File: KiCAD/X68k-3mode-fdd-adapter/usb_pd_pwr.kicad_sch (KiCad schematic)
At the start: 27 parts, among them J1001 Barrel_Jack_Switch, J1002 USB_C_Receptacle_USB2.0_16P, Q1001 FDS4935A, Q1002 FDS4935A, Q1003 FDS4935A, U1001 K7805M-1000R3, U1002 MCP1792x-5002xCB

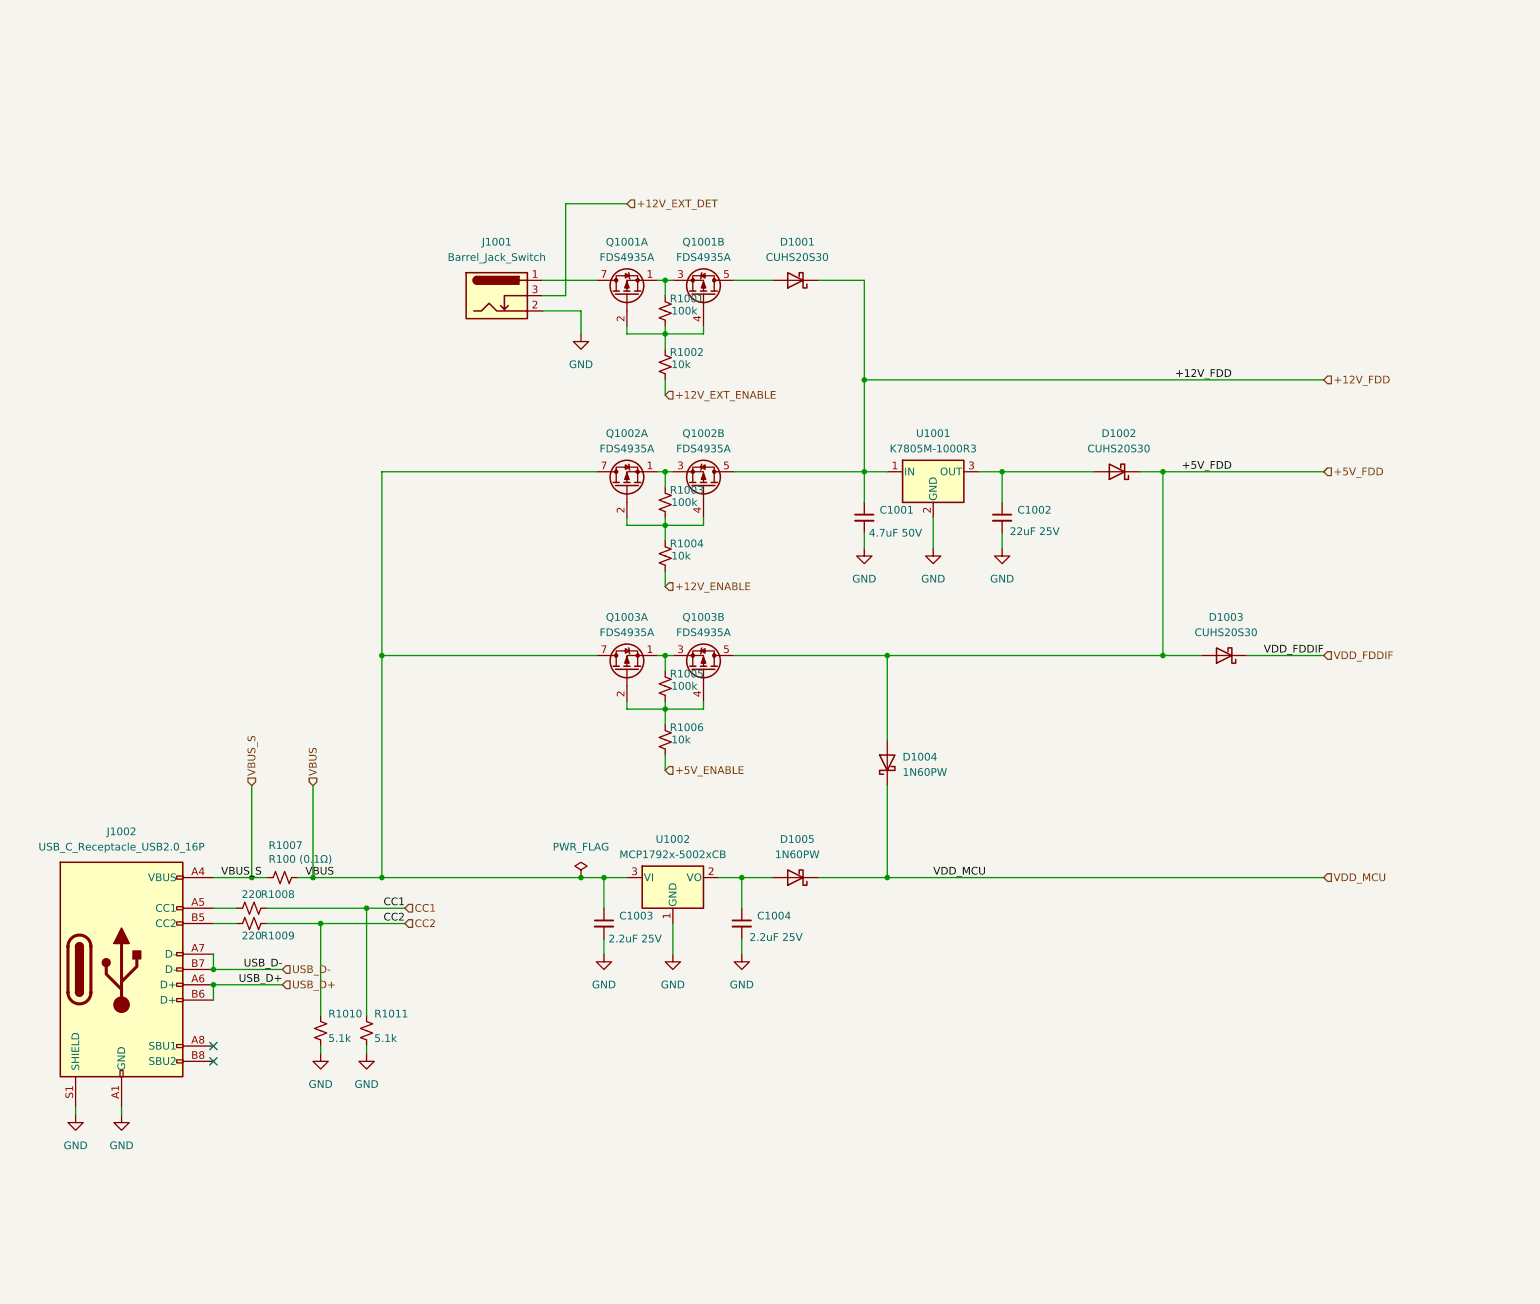
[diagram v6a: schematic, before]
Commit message: 電源周りの回路を修正
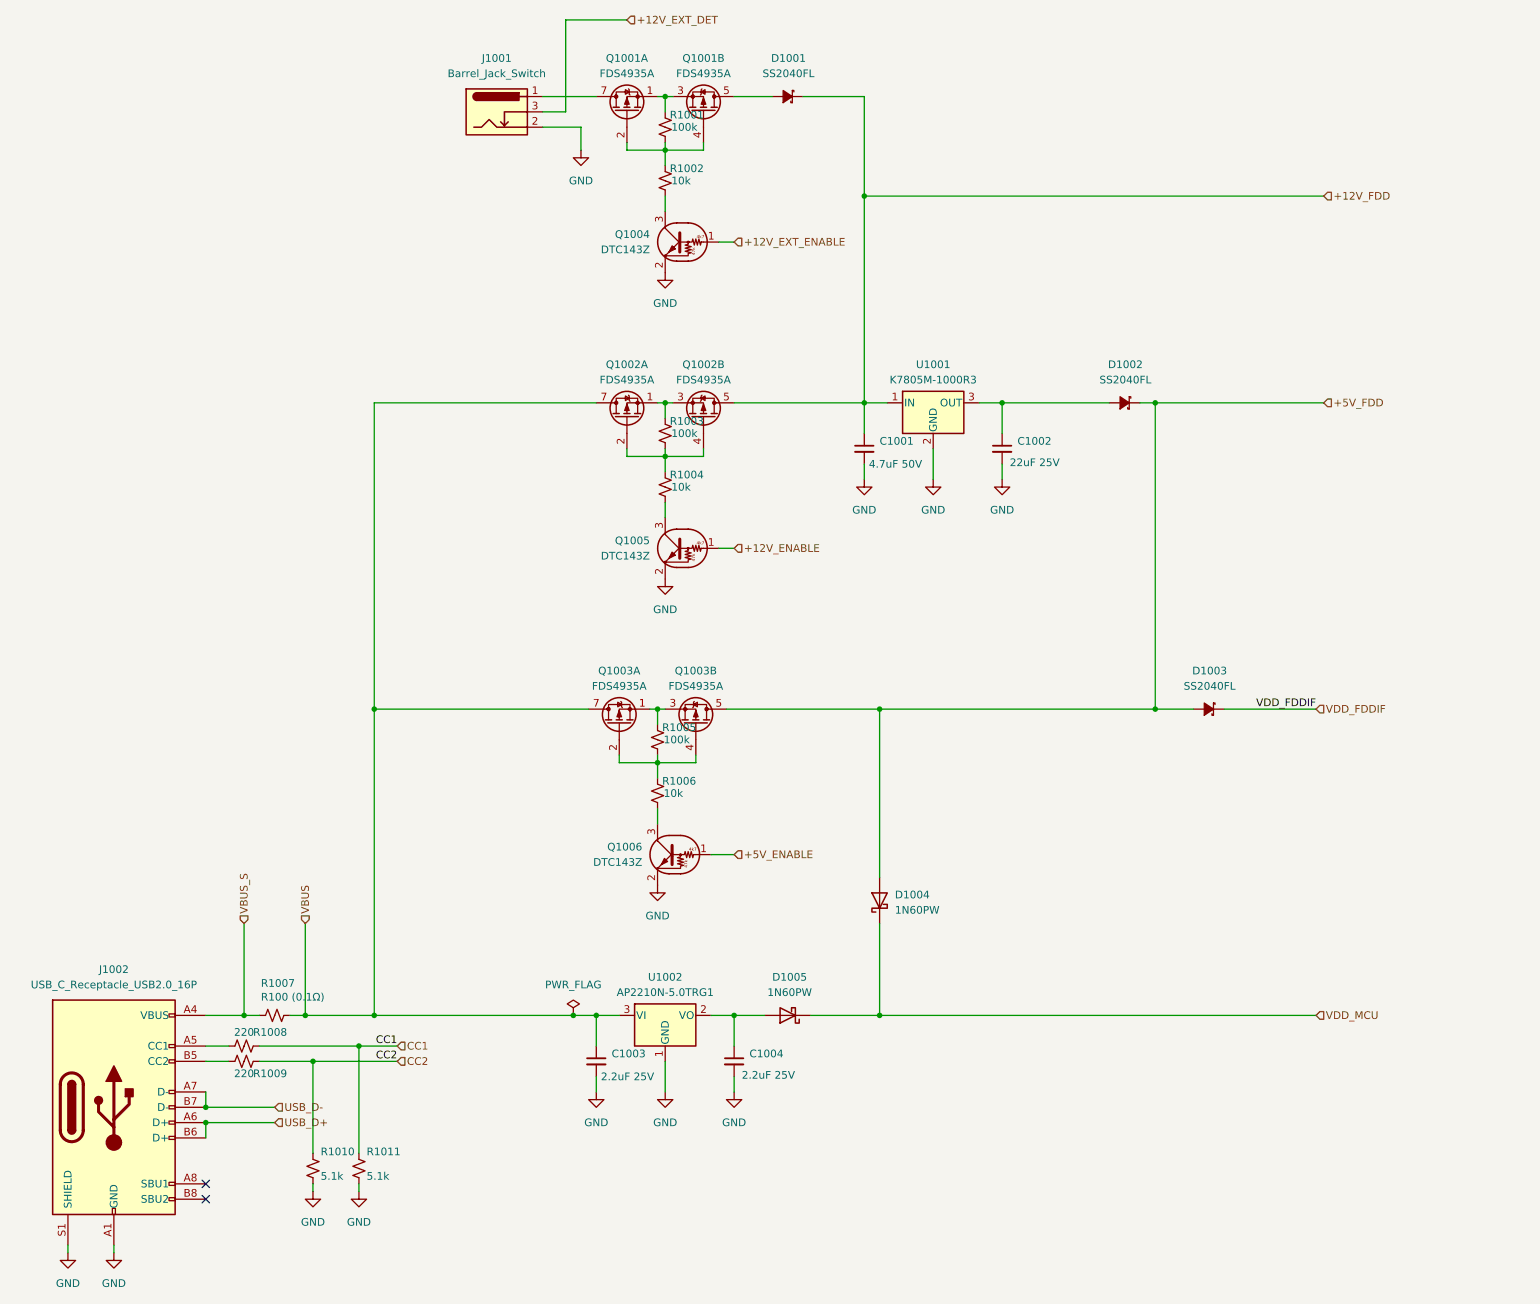
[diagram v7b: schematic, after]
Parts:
- removed D1001, D1002, D1003: CUHS20S30, x68k-lib:CUHS20S30 (US2H), symbol Device:D_Schottky
- added D1001, D1002, D1003: SS2040FL, Diode_SMD:D_SOD-123F, symbol x68000-ext:SS2040FL
- added Q1004, Q1005, Q1006: DTC143Z, Package_TO_SOT_SMD:SOT-523, symbol x68000-ext:DTC143Z
- C1004: LCSC (none) -> C19110
- U1002: value MCP1792x-5002xCB -> AP2210N-5.0TRG1; symbol Regulator_Linear:MCP1792x-5002xCB -> x68000-ext:AP2210N-5.0TRG1; LCSC (none) -> C460341
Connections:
- net +12V_ENABLE: now also Q1005.1 (B); no longer R1004.2
- net +12V_EXT_ENABLE: now also Q1004.1 (B); no longer R1002.2
- net +12V_FDD: now also D1001.1 (K)
- net +5V_ENABLE: now also Q1006.1 (B); no longer R1006.2
- net +5V_FDD: now also D1002.1 (K), D1003.2 (A)
- net GND: now also Q1004.2 (E), Q1005.2 (E), Q1006.2 (E)
- net VDD_FDDIF: now also D1003.1 (K)
- net at C1002.1, U1001.3 (OUT): now also D1002.2 (A)
- net at Q1001.5 (D2), Q1001.6 (D2): now also D1001.2 (A)
- new net: Q1004.3 (C), R1002.2
- new net: Q1006.3 (C), R1006.2
- new net: Q1005.3 (C), R1004.2
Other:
- moved on the sheet: C1001, C1002, C1003, C1004, D1004, D1005, J1001, J1002, Q1001A, Q1001B, Q1002A, Q1002B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

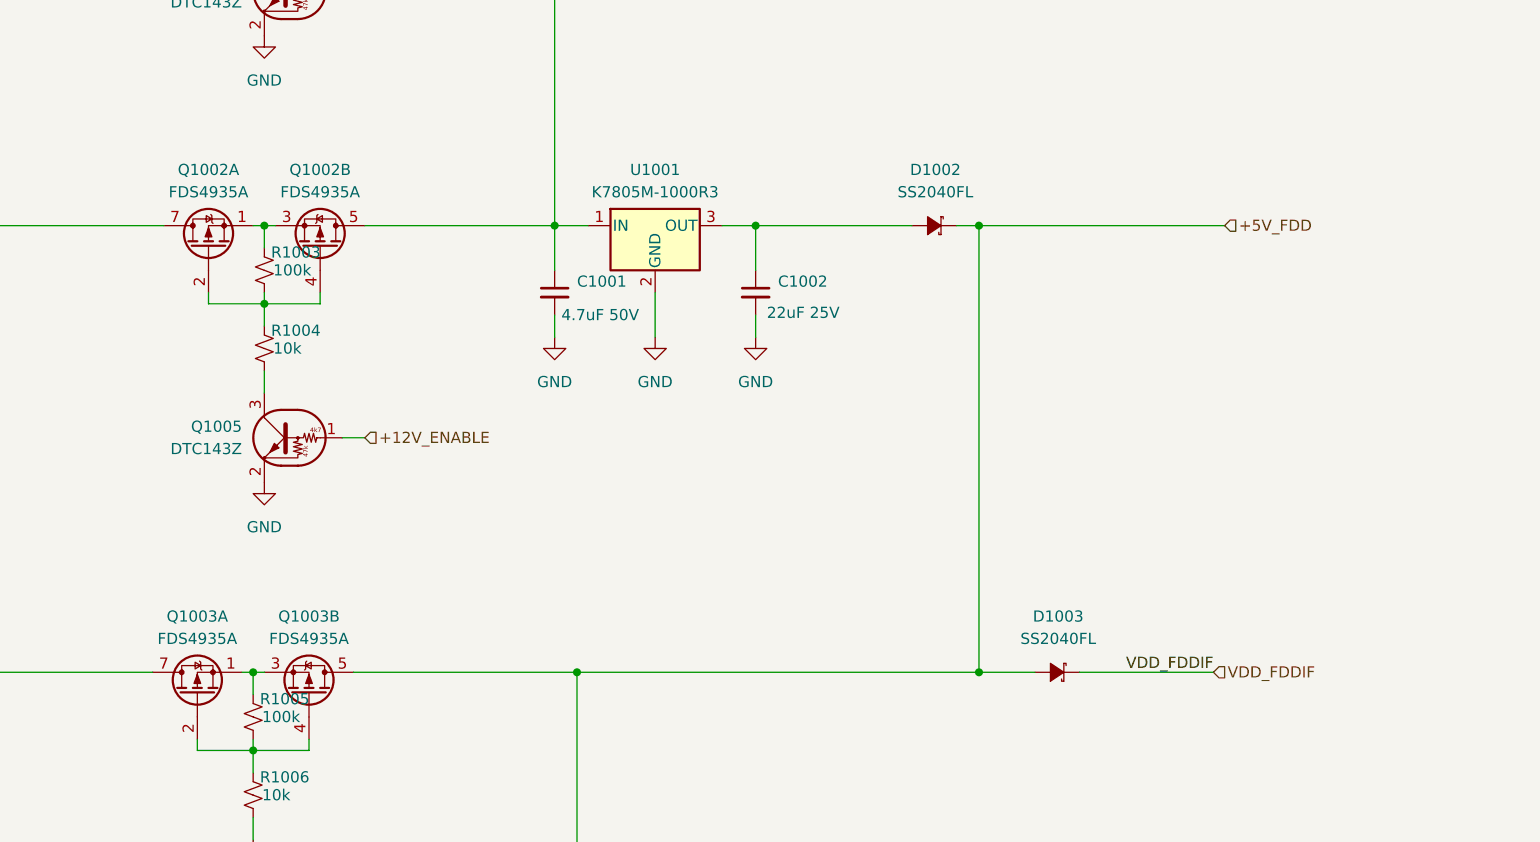
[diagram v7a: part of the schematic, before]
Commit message: * DCDCの出力の直後のダイオードをFETに変更 * DriveSelectのAとBが逆に配線されていた問題を修正
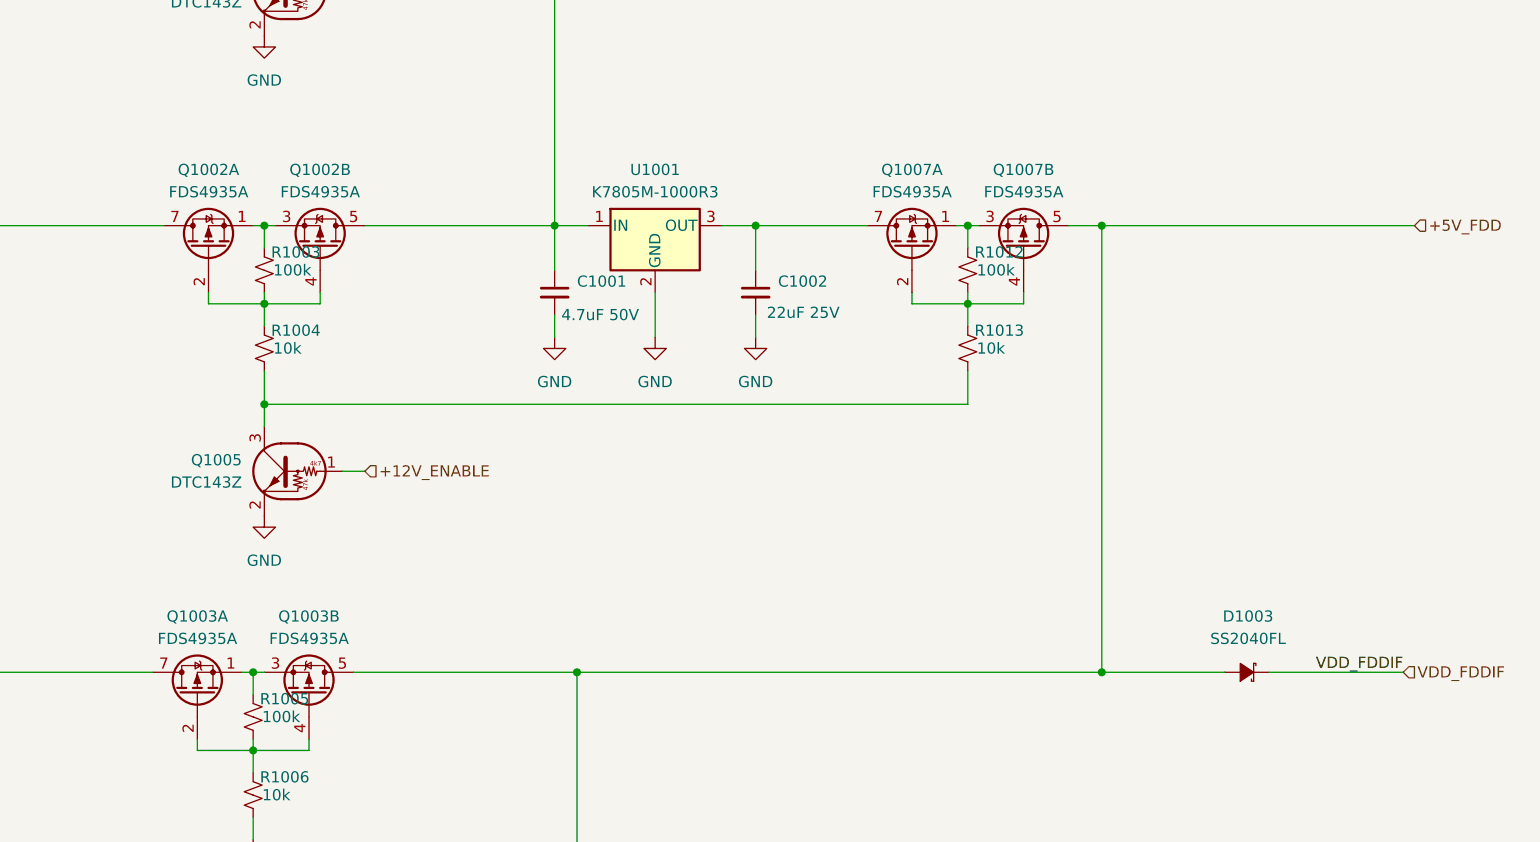
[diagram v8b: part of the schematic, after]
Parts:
- removed D1002: SS2040FL, Diode_SMD:D_SOD-123F, symbol x68000-ext:SS2040FL
- added Q1007: FDS4935A, Package_SO:SOIC-8_3.9x4.9mm_P1.27mm, symbol x68000-ext:FDS4935A
- added R1012: 100k, Resistor_SMD:R_0603_1608Metric, symbol Device:R_Small_US
- added R1013: 10k, Resistor_SMD:R_0603_1608Metric, symbol Device:R_Small_US
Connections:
- net +5V_FDD: now also Q1007.5 (D2), Q1007.6 (D2)
- net at C1002.1, U1001.3 (OUT): now also Q1007.7 (D2), Q1007.8 (D2)
- net at Q1005.3 (C), R1004.2: now also R1013.2
- new net: Q1007.1 (S2), Q1007.3 (S2), R1012.1
- new net: Q1007.2 (G2), Q1007.4 (G2), R1012.2, R1013.1
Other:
- moved on the sheet: D1003, Q1005
